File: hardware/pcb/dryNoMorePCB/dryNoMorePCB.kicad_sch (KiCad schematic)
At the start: 46 parts, among them J1 USB_A_Stacked, J10 Barrel_Jack_MountingPin, J11 Conn_01x03, J12 Conn_01x03, J13 Conn_01x02, J14 ETH_W5500, J15 Conn_01x02, J16 Conn_01x02, J17 Conn_01x02, J18 GND, J19 GND, J2 Conn_01x03, J20 +5V, J21 +5V, J3 Conn_01x03, J4 Conn_01x03, J5 USB_A_Stacked, J6 Conn_01x03, J7 Conn_01x03, J8 Conn_01x03, J9 USB_A_Stacked, Q1 Q_NMOS_GDSD, Q2 Q_NMOS_GDSD, Q3 Q_NMOS_GDSD, Q4 Q_NMOS_GDSD, Q5 Q_NMOS_GDSD, Q6 Q_NMOS_GDSD, U1 74HC595, U2 74HC595

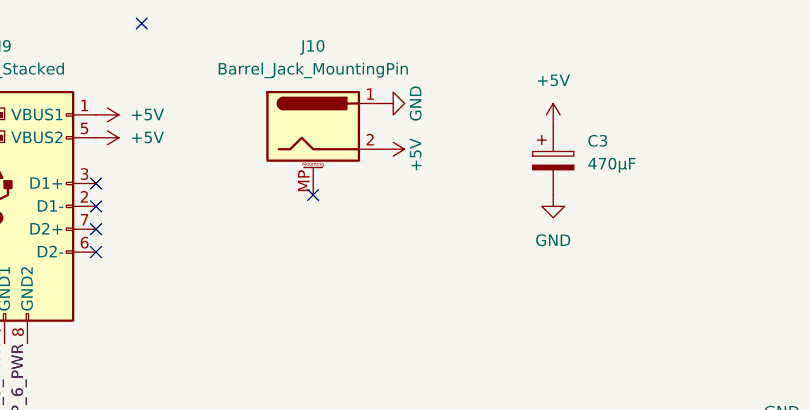
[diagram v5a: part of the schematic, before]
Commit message: hardware: fix input voltage polarity (J10), pump version
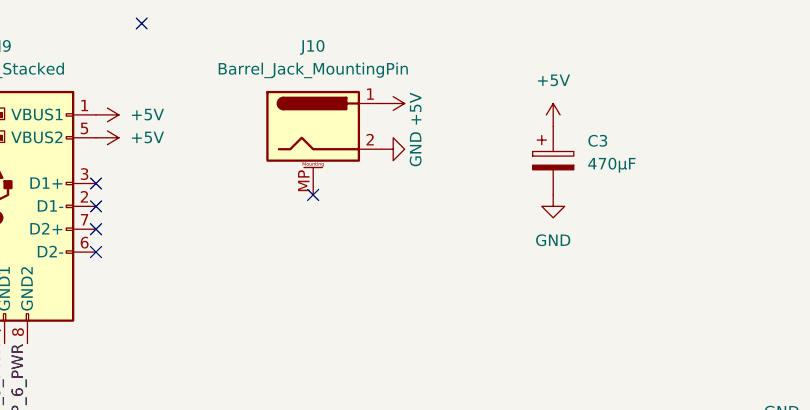
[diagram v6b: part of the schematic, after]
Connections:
- net +5V: now also J10.1; no longer J10.2
- net GND: now also J10.2; no longer J10.1
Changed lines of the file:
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@@
     (title "DryNoMorePCB by 7FM")
     (date "2022-07-16")
-    (rev "v0.1")
+    (rev "v0.2")
   )
   (junction (at 66.04 184.15) (diameter 0) (color 0 0 0 0)
@@
     (pin "1")
   )
-  (symbol (lib_id "power:GND") (at 120.65 20.32 90) (unit 1)
+  (symbol (lib_id "power:GND") (at 120.65 25.4 90) (unit 1)
     (in_bom yes) (on_board yes)
-    (property "Reference" "#PWR038" (id 0) (at 127 20.32 0)
-      (effects (font (size 1.27 1.27)) hide)
-    )
-    (property "Value" "GND" (id 1) (at 124.46 20.32 0))
-    (property "Footprint" "" (id 2) (at 120.65 20.32 0)
-      (effects (font (size 1.27 1.27)) hide)
-    )
-    (property "Datasheet" "" (id 3) (at 120.65 20.32 0)
+    (property "Reference" "#PWR038" (id 0) (at 127 25.4 0)
+      (effects (font (size 1.27 1.27)) hide)
+    )
+    (property "Value" "GND" (id 1) (at 124.46 25.4 0))
+    (property "Footprint" "" (id 2) (at 120.65 25.4 0)
+      (effects (font (size 1.27 1.27)) hide)
+    )
+    (property "Datasheet" "" (id 3) (at 120.65 25.4 0)
       (effects (font (size 1.27 1.27)) hide)
     )
@@
     (pin "1")
   )
-  (symbol (lib_id "power:+5V") (at 120.65 25.4 270) (unit 1)
+  (symbol (lib_id "power:+5V") (at 120.65 20.32 270) (unit 1)
     (in_bom yes) (on_board yes)
-    (property "Reference" "#PWR039" (id 0) (at 116.84 25.4 0)
-      (effects (font (size 1.27 1.27)) hide)
-    )
-    (property "Value" "+5V" (id 1) (at 124.46 27.94 0)
-      (effects (font (size 1.27 1.27)) (justify right))
-    )
-    (property "Footprint" "" (id 2) (at 120.65 25.4 0)
-      (effects (font (size 1.27 1.27)) hide)
-    )
-    (property "Datasheet" "" (id 3) (at 120.65 25.4 0)
-      (effects (font (size 1.27 1.27)) hide)
-    )
+    (property "Reference" "#PWR039" (id 0) (at 116.84 20.32 0)
+      (effects (font (size 1.27 1.27)) hide)
+    )
+    (property "Value" "+5V" (id 1) (at 124.46 22.86 0)
+      (effects (font (size 1.27 1.27)) (justify right))
+    )
+    (property "Footprint" "" (id 2) (at 120.65 20.32 0)
+      (effects (font (size 1.27 1.27)) hide)
+    )
+    (property "Datasheet" "" (id 3) (at 120.65 20.32 0)
+      (effects (font (size 1.27 1.27)) hide)
+    )

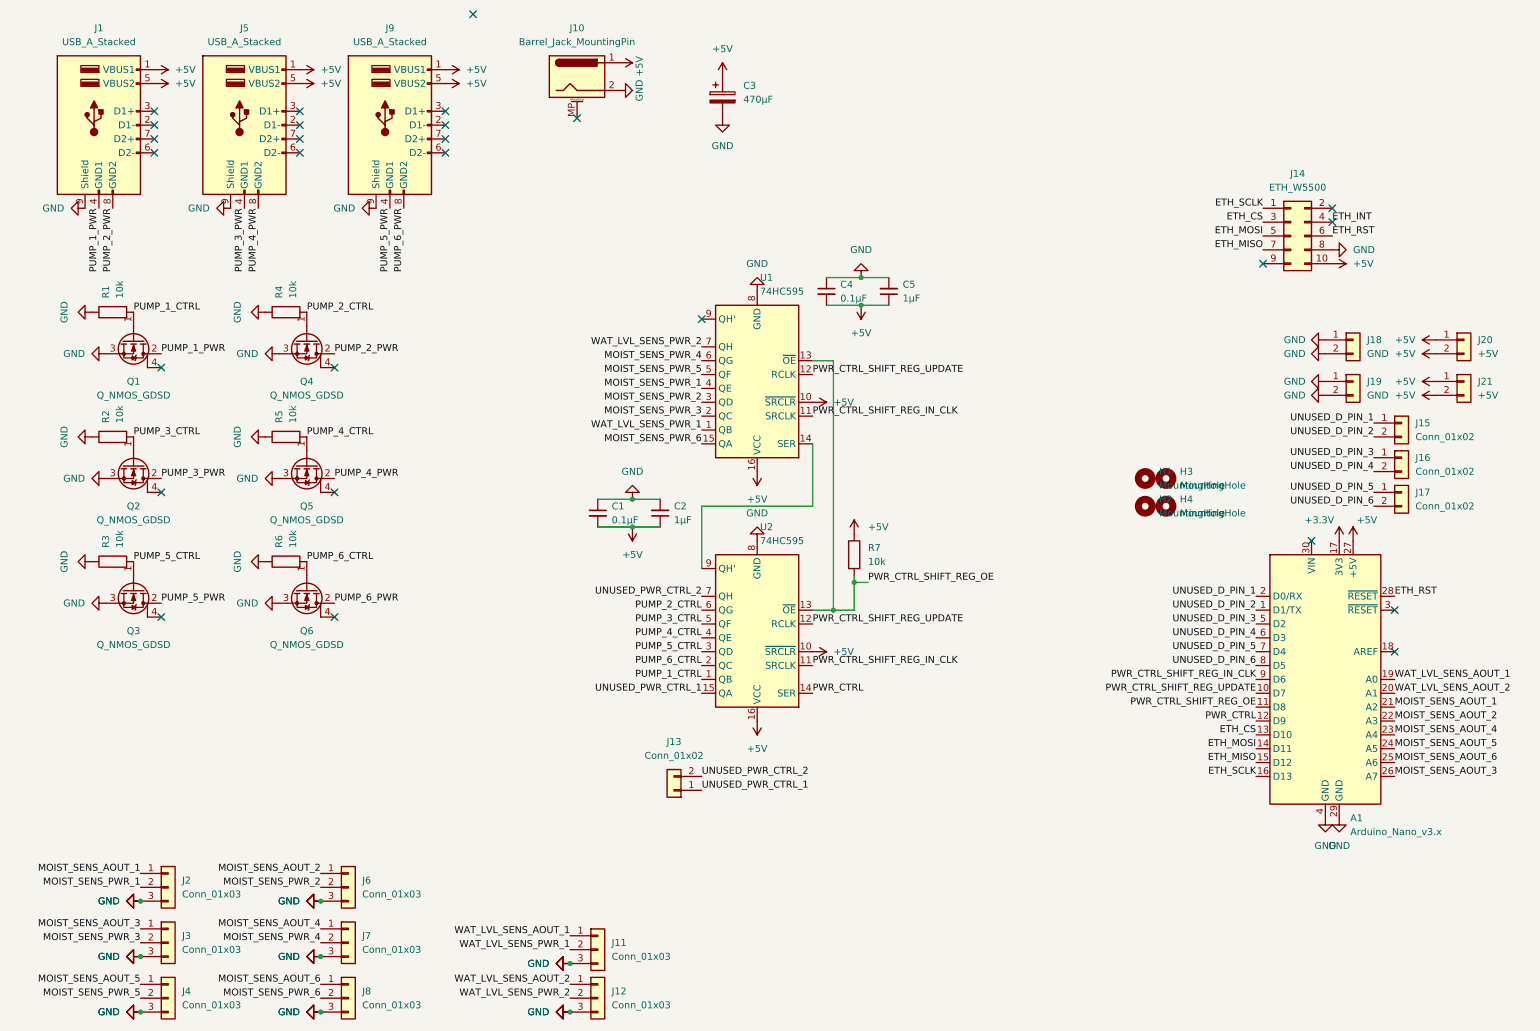
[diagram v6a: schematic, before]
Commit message: new hardware revision: add mosfet to switch off the ethernet module
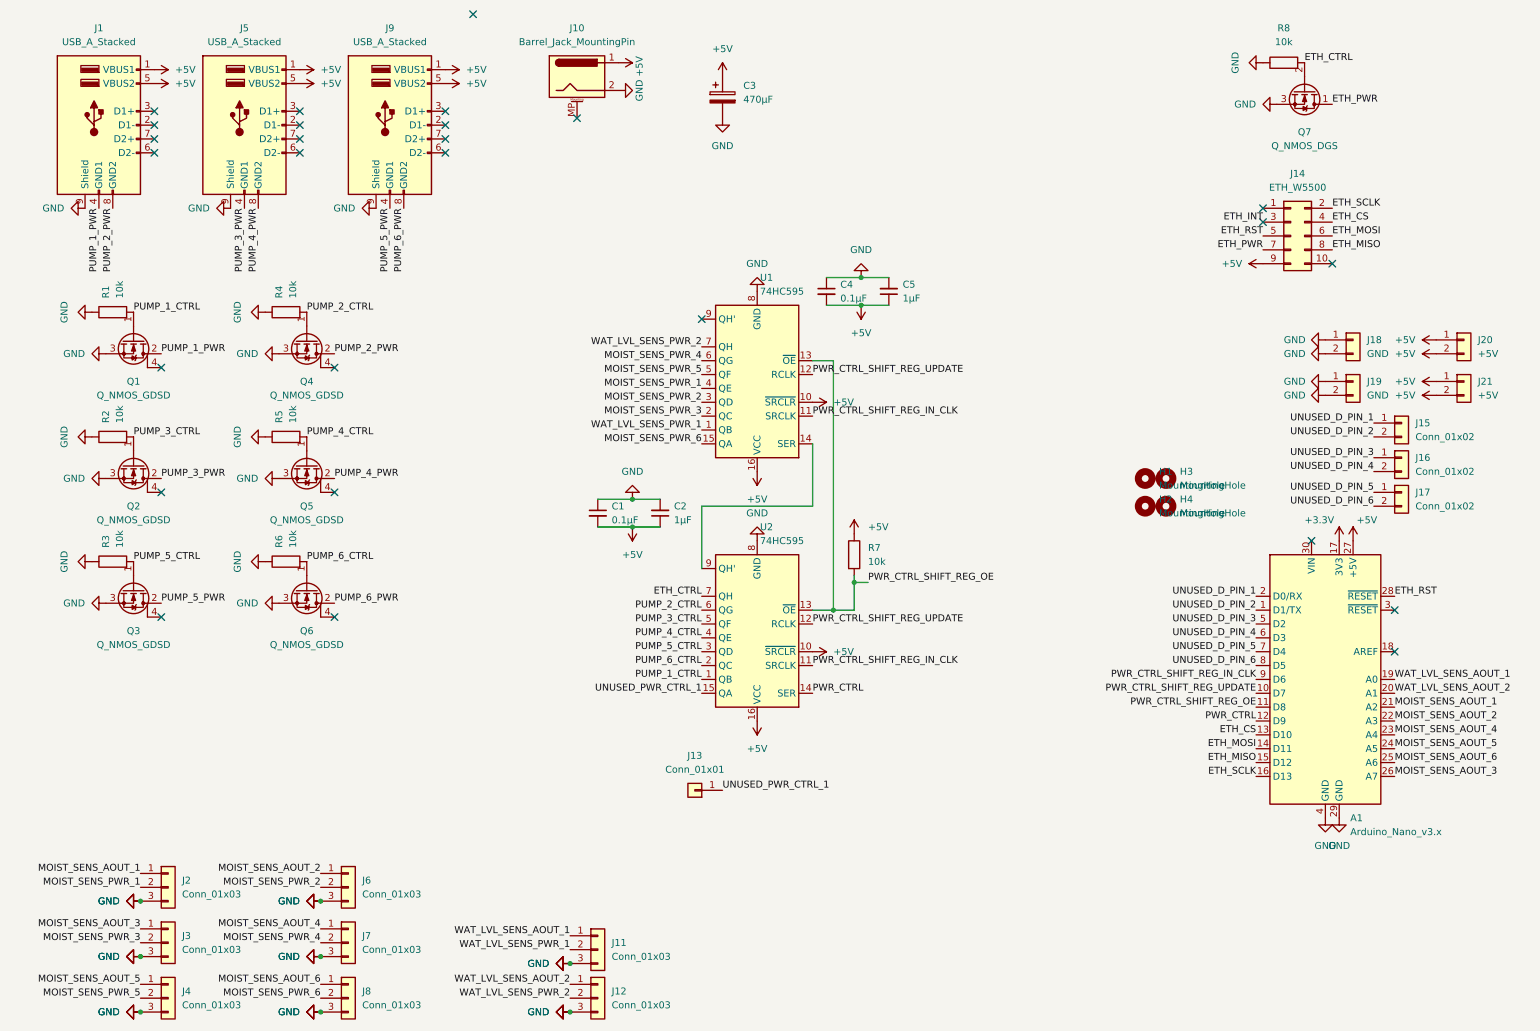
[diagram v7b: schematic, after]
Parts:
- removed J13: Conn_01x02, Connector_PinHeader_2.54mm:PinHeader_1x02_P2.54mm_Vertical, symbol Connector_Generic:Conn_01x02
- added J13: Conn_01x01, Connector_PinHeader_2.54mm:PinHeader_1x01_P2.54mm_Vertical, symbol Connector_Generic:Conn_01x01
- added Q7: Q_NMOS_DGS, Package_TO_SOT_THT:TO-92_Inline, symbol Device:Q_NMOS_DGS
- added R8: 10k, Resistor_THT:R_Axial_DIN0207_L6.3mm_D2.5mm_P2.54mm_Vertical, symbol Device:R
- J14: footprint Connector_PinHeader_2.54mm:PinHeader_2x05_P2.54mm_Vertical -> Connector_PinSocket_2.54mm:PinSocket_2x05_P2.54mm_Vertical
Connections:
- net +5V: now also J14.9 (Pin_9); no longer J14.10 (Pin_10)
- net ETH_CS: now also J14.4 (Pin_4); no longer J14.3 (Pin_3)
- net ETH_INT: now also J14.3 (Pin_3); no longer J14.4 (Pin_4)
- net ETH_MISO: now also J14.8 (Pin_8); no longer J14.7 (Pin_7)
- net ETH_MOSI: now also J14.6 (Pin_6); no longer J14.5 (Pin_5)
- net ETH_RST: now also J14.5 (Pin_5); no longer J14.6 (Pin_6)
- net ETH_SCLK: now also J14.2 (Pin_2); no longer J14.1 (Pin_1)
- net GND: now also Q7.3 (S), R8.1; no longer J14.8 (Pin_8)
- net UNUSED_PWR_CTRL_1: now also J13.1 (Pin_1)
- net UNUSED_PWR_CTRL_2 renamed ETH_CTRL
- net ETH_CTRL: now also Q7.2 (G), R8.2
- new net ETH_PWR: J14.7 (Pin_7), Q7.1 (D)

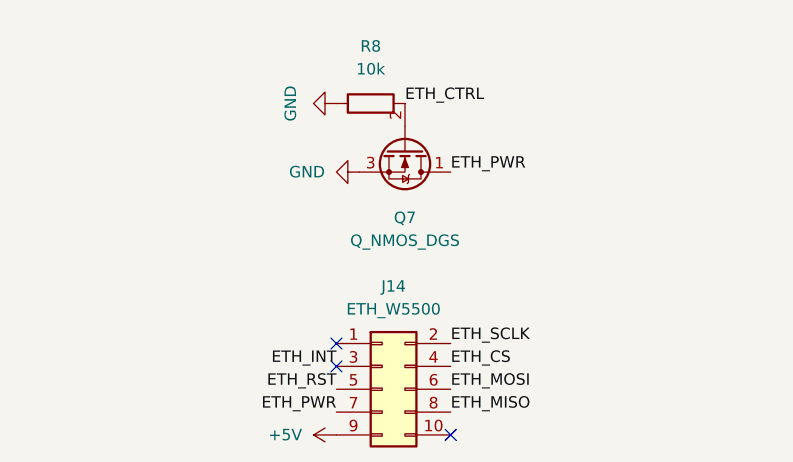
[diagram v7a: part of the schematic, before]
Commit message: change nmos from DGS to SGD pinout to match an 2N7000
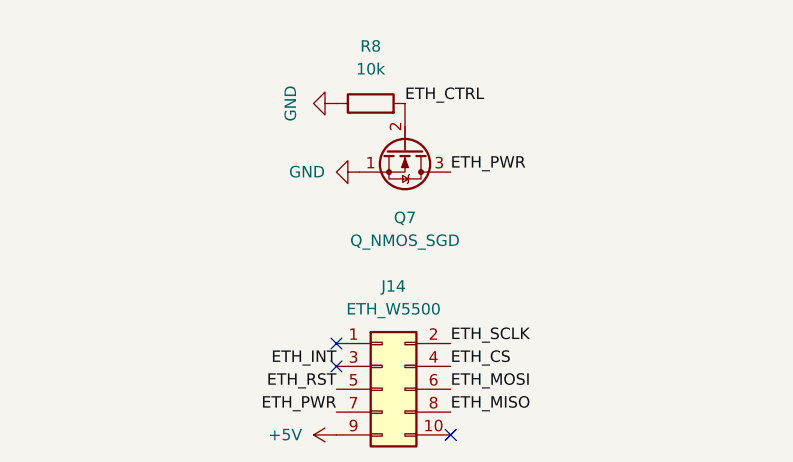
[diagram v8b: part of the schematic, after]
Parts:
- removed Q7: Q_NMOS_DGS, Package_TO_SOT_THT:TO-92_Inline, symbol Device:Q_NMOS_DGS
- added Q7: Q_NMOS_SGD, Package_TO_SOT_THT:TO-92_Inline, symbol Device:Q_NMOS_SGD
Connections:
- net ETH_CTRL: now also Q7.2 (G)
- net ETH_PWR: now also Q7.3 (D)
- net GND: now also Q7.1 (S)
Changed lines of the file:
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@@
     (pin "1")
+  )
+  (symbol (lib_id "Device:Q_NMOS_SGD") (at 246.38 25.4 270) (unit 1)
+    (in_bom yes) (on_board yes) (fields_autoplaced)
+    (property "Reference" "Q7" (id 0) (at 246.38 33.02 90))
+    (property "Value" "Q_NMOS_SGD" (id 1) (at 246.38 35.56 90))
+    (property "Footprint" "Package_TO_SOT_THT:TO-92_Inline" (id 2) (at 248.92 30.48 0)
+      (effects (font (size 1.27 1.27)) hide)
+    )
+    (property "Datasheet" "~" (id 3) (at 246.38 25.4 0)
+      (effects (font (size 1.27 1.27)) hide)
+    )
+    (pin "1")
+    (pin "2")
+    (pin "3")
   )
   (symbol (lib_id "Device:Q_NMOS_GDSD") (at 63.5 116.84 270) (unit 1)
@@
     )
     (pin "1")
-  )
-  (symbol (lib_id "Device:Q_NMOS_DGS") (at 246.38 25.4 270) (unit 1)
-    (in_bom yes) (on_board yes) (fields_autoplaced)
-    (property "Reference" "Q7" (id 0) (at 246.38 33.02 90))
-    (property "Value" "Q_NMOS_DGS" (id 1) (at 246.38 35.56 90))
-    (property "Footprint" "Package_TO_SOT_THT:TO-92_Inline" (id 2) (at 248.92 30.48 0)
-      (effects (font (size 1.27 1.27)) hide)
-    )
-    (property "Datasheet" "~" (id 3) (at 246.38 25.4 0)
-      (effects (font (size 1.27 1.27)) hide)
-    )
-    (pin "1")
-    (pin "2")
-    (pin "3")
   )
   (symbol (lib_id "power:+5V") (at 139.7 22.86 0) (unit 1)
@@
       (reference "Q6") (unit 1) (value "Q_NMOS_GDSD") (footprint "Package_TO_SOT_THT:TO-220-3_Vertical")
     )
-    (path "/684e04e2-95db-4726-a774-77a3f8fcf1b5"
-      (reference "Q7") (unit 1) (value "Q_NMOS_DGS") (footprint "Package_TO_SOT_THT:TO-92_Inline")
+    (path "/29a6f446-b615-46e4-b0b2-7e3068f56e55"
+      (reference "Q7") (unit 1) (value "Q_NMOS_SGD") (footprint "Package_TO_SOT_THT:TO-92_Inline")
     )
     (path "/9d6ce5a1-6f1e-400f-89a2-d850d915a1d7"
